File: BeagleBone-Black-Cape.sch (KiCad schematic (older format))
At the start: 2 parts, among them P8 BeagleBone_Black_Header, P9 BeagleBone_Black_Header

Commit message: Added Buttons, LEDs and MCU to BB connections.
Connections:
- net labels added: BB_BTN_1, BB_BTN_2, PWR_BTN, ZNP_RX, ZNP_TX
- net labels removed: PWR_BUT
- wire segments 39 -> 43
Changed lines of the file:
@@
 	2450 1800 2550 1800
 Text GLabel 1850 1800 0    50   Input ~ 0
-PWR_BUT
+PWR_BTN
 Wire Wire Line
 	1950 1800 1850 1800
@@
 F1 "CrystolOscillator.sch" 50
 $EndSheet
+Text GLabel 1850 1900 0    50   Input ~ 0
+ZNP_TX
+Text GLabel 1850 2000 0    50   Input ~ 0
+ZNP_RX
+Wire Wire Line
+	1850 1900 1950 1900
+Wire Wire Line
+	1850 2000 1950 2000
+Text GLabel 2550 2000 2    50   Input ~ 0
+BB_BTN_1
+Text GLabel 2550 2100 2    50   Input ~ 0
+BB_BTN_2
+Wire Wire Line
+	2550 2000 2450 2000
+Wire Wire Line
+	2550 2100 2450 2100
 $EndSCHEMATC

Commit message: part way through getting new ICs and other components back on the PCB
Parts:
- renumbered P9 to P101, P8 to P102
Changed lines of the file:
@@
 $EndDescr
 $Comp
-L BeagleBone-Black-Cape-rescue:GNDD-power #PWR01
+L BeagleBone-Black-Cape-rescue:GNDD-power #PWR0105
 U 1 1 5589785A
 P 2200 3900
-F 0 "#PWR01" H 2200 3650 50  0001 C CNN
+F 0 "#PWR0105" H 2200 3650 50  0001 C CNN
 F 1 "GNDD" H 2200 3750 50  0000 C CNN
 F 2 "" H 2200 3900 60  0000 C CNN
@@
 Connection ~ 2200 3800
 $Comp
-L BeagleBone-Black-Cape-rescue:GNDD-power #PWR02
+L BeagleBone-Black-Cape-rescue:GNDD-power #PWR0111
 U 1 1 558978D3
 P 3250 1400
-F 0 "#PWR02" H 3250 1150 50  0001 C CNN
+F 0 "#PWR0111" H 3250 1150 50  0001 C CNN
 F 1 "GNDD" H 3250 1250 50  0000 C CNN
 F 2 "" H 3250 1400 60  0000 C CNN
@@
 $EndComp
 $Comp
-L BeagleBone-Black-Cape-rescue:GNDD-power #PWR03
+L BeagleBone-Black-Cape-rescue:GNDD-power #PWR0101
 U 1 1 5589790A
 P 1150 1400
-F 0 "#PWR03" H 1150 1150 50  0001 C CNN
+F 0 "#PWR0101" H 1150 1150 50  0001 C CNN
 F 1 "GNDD" H 1150 1250 50  0000 C CNN
 F 2 "" H 1150 1400 60  0000 C CNN
@@
 $EndComp
 $Comp
-L BeagleBone-Black-Cape-rescue:GNDD-power #PWR04
+L BeagleBone-Black-Cape-rescue:GNDD-power #PWR0112
 U 1 1 558979C1
 P 9850 750
-F 0 "#PWR04" H 9850 500 50  0001 C CNN
+F 0 "#PWR0112" H 9850 500 50  0001 C CNN
 F 1 "GNDD" H 9850 600 50  0000 C CNN
 F 2 "" H 9850 750 60  0000 C CNN
@@
 $EndComp
 $Comp
-L BeagleBone-Black-Cape-rescue:GNDD-power #PWR05
+L BeagleBone-Black-Cape-rescue:GNDD-power #PWR0113
 U 1 1 558979E8
 P 10850 750
-F 0 "#PWR05" H 10850 500 50  0001 C CNN
+F 0 "#PWR0113" H 10850 500 50  0001 C CNN
 F 1 "GNDD" H 10850 600 50  0000 C CNN
 F 2 "" H 10850 750 60  0000 C CNN
@@
 $EndComp
 $Comp
-L BeagleBone-Black-Cape-rescue:+3.3V-power #PWR06
+L BeagleBone-Black-Cape-rescue:+3.3V-power #PWR0106
 U 1 1 55897A67
 P 2600 1200
-F 0 "#PWR06" H 2600 1050 50  0001 C CNN
+F 0 "#PWR0106" H 2600 1050 50  0001 C CNN
 F 1 "+3V3" H 2600 1340 50  0000 C CNN
 F 2 "" H 2600 1200 60  0000 C CNN
@@
 $EndComp
 $Comp
-L BeagleBone-Black-Cape-rescue:+5V-power #PWR07
+L BeagleBone-Black-Cape-rescue:+5V-power #PWR0107
 U 1 1 55897A7F
 P 2800 1200
-F 0 "#PWR07" H 2800 1050 50  0001 C CNN
+F 0 "#PWR0107" H 2800 1050 50  0001 C CNN
 F 1 "+5V" H 2800 1340 50  0000 C CNN
 F 2 "" H 2800 1200 60  0000 C CNN
@@
 	3050 1700 2450 1700
 $Comp
-L BeagleBone-Black-Cape-rescue:+3.3V-power #PWR08
+L BeagleBone-Black-Cape-rescue:+3.3V-power #PWR0104
 U 1 1 55897EE7
 P 1800 1200
-F 0 "#PWR08" H 1800 1050 50  0001 C CNN
+F 0 "#PWR0104" H 1800 1050 50  0001 C CNN
 F 1 "+3V3" H 1800 1340 50  0000 C CNN
 F 2 "" H 1800 1200 60  0000 C CNN
@@
 $EndComp
 $Comp
-L BeagleBone-Black-Cape-rescue:+5V-power #PWR09
+L BeagleBone-Black-Cape-rescue:+5V-power #PWR0103
 U 1 1 55897EF8
 P 1600 1200
-F 0 "#PWR09" H 1600 1050 50  0001 C CNN
+F 0 "#PWR0103" H 1600 1050 50  0001 C CNN
 F 1 "+5V" H 1600 1340 50  0000 C CNN
 F 2 "" H 1600 1200 60  0000 C CNN
@@
 	10600 750  10850 750
 $Comp
-L pwr_BeagleBone:SYS_5V #PWR010
+L pwr_BeagleBone:SYS_5V #PWR0110
 U 1 1 55898497
 P 3050 1200
-F 0 "#PWR010" H 3050 1050 50  0001 C CNN
+F 0 "#PWR0110" H 3050 1050 50  0001 C CNN
 F 1 "SYS_5V" H 3050 1340 50  0000 C CNN
 F 2 "" H 3050 1200 60  0000 C CNN
@@
 $EndComp
 $Comp
-L pwr_BeagleBone:SYS_5V #PWR011
+L pwr_BeagleBone:SYS_5V #PWR0102
 U 1 1 558984AF
 P 1350 1200
-F 0 "#PWR011" H 1350 1050 50  0001 C CNN
+F 0 "#PWR0102" H 1350 1050 50  0001 C CNN
 F 1 "SYS_5V" H 1350 1340 50  0000 C CNN
 F 2 "" H 1350 1200 60  0000 C CNN
@@
 	2450 2900 2800 2900
 $Comp
-L pwr_BeagleBone:GNDA_ADC #PWR013
+L pwr_BeagleBone:GNDA_ADC #PWR0109
 U 1 1 5589865D
 P 2800 3000
-F 0 "#PWR013" H 2800 2750 50  0001 C CNN
+F 0 "#PWR0109" H 2800 2750 50  0001 C CNN
 F 1 "GNDA_ADC" H 2700 2850 50  0000 C CNN
 F 2 "" H 2800 3000 60  0000 C CNN
@@
 	1950 1800 1850 1800
 $Comp
-L BeagleBone-Black-Cape-rescue:Conn_02x23_Odd_Even-Connector_Generic P9
+L BeagleBone-Black-Cape-rescue:Conn_02x23_Odd_Even-Connector_Generic P101
 U 1 1 55DF7DBA
 P 2150 2500
-F 0 "P9" H 2150 3700 50  0000 C CNN
+F 0 "P101" H 2150 3700 50  0000 C CNN
 F 1 "BeagleBone_Black_Header" V 2200 2550 50  0000 C CNN
 F 2 "Socket_BeagleBone_Black:Socket_BeagleBone_Black" H 2150 1650 60  0001 C CNN
@@
 $EndComp
 $Comp
-L BeagleBone-Black-Cape-rescue:Conn_02x23_Odd_Even-Connector_Generic P8
+L BeagleBone-Black-Cape-rescue:Conn_02x23_Odd_Even-Connector_Generic P102
 U 1 1 55DF7DE1
 P 10300 1850
-F 0 "P8" H 10300 3050 50  0000 C CNN
+F 0 "P102" H 10300 3050 50  0000 C CNN
 F 1 "BeagleBone_Black_Header" V 10350 1900 50  0000 C CNN
 F 2 "Socket_BeagleBone_Black:Socket_BeagleBone_Black" H 10300 1000 60  0001 C CNN
@@
 MOSI_TFT
 $Comp
-L pwr_BeagleBone:VDD_ADC #PWR012
+L pwr_BeagleBone:VDD_ADC #PWR0108
 U 1 1 558985D8
 P 2800 2900
-F 0 "#PWR012" H 2800 2750 50  0001 C CNN
+F 0 "#PWR0108" H 2800 2750 50  0001 C CNN
 F 1 "VDD_ADC" H 2800 3150 50  0000 C CNN
 F 2 "" H 2800 2900 60  0000 C CNN

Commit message: Added UI buttons, LEDs, Decoupling caps, MCU connections, and other good stuff.
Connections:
- net labels added: GND
- net labels removed: GND8, GNDA_ADC, GNDD, VDD_ADC
- wire segments 43 -> 38
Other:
- moved on the sheet: P101, P102

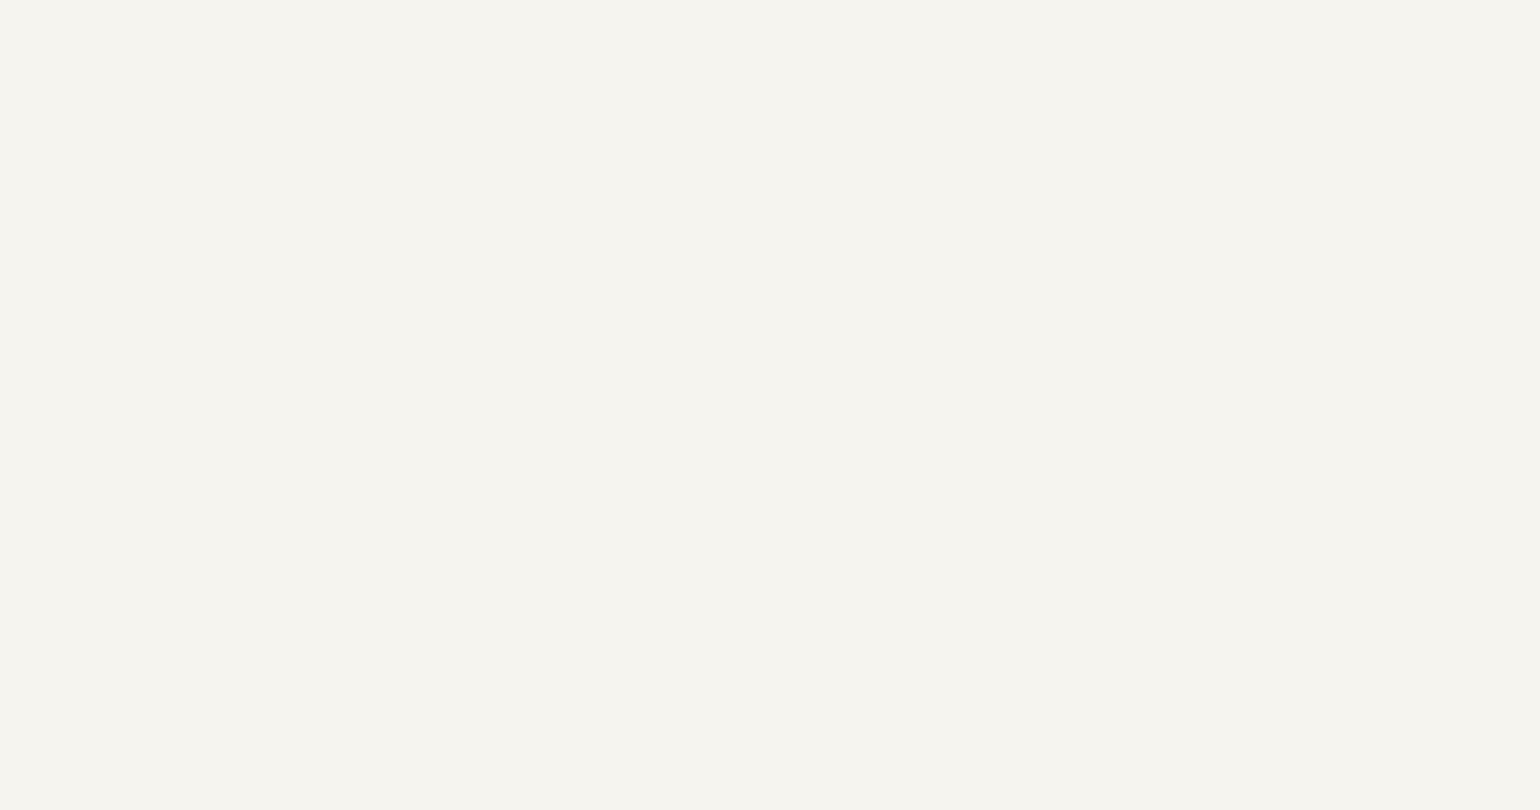
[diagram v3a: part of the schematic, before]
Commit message: Moved MCU to its own sheet.
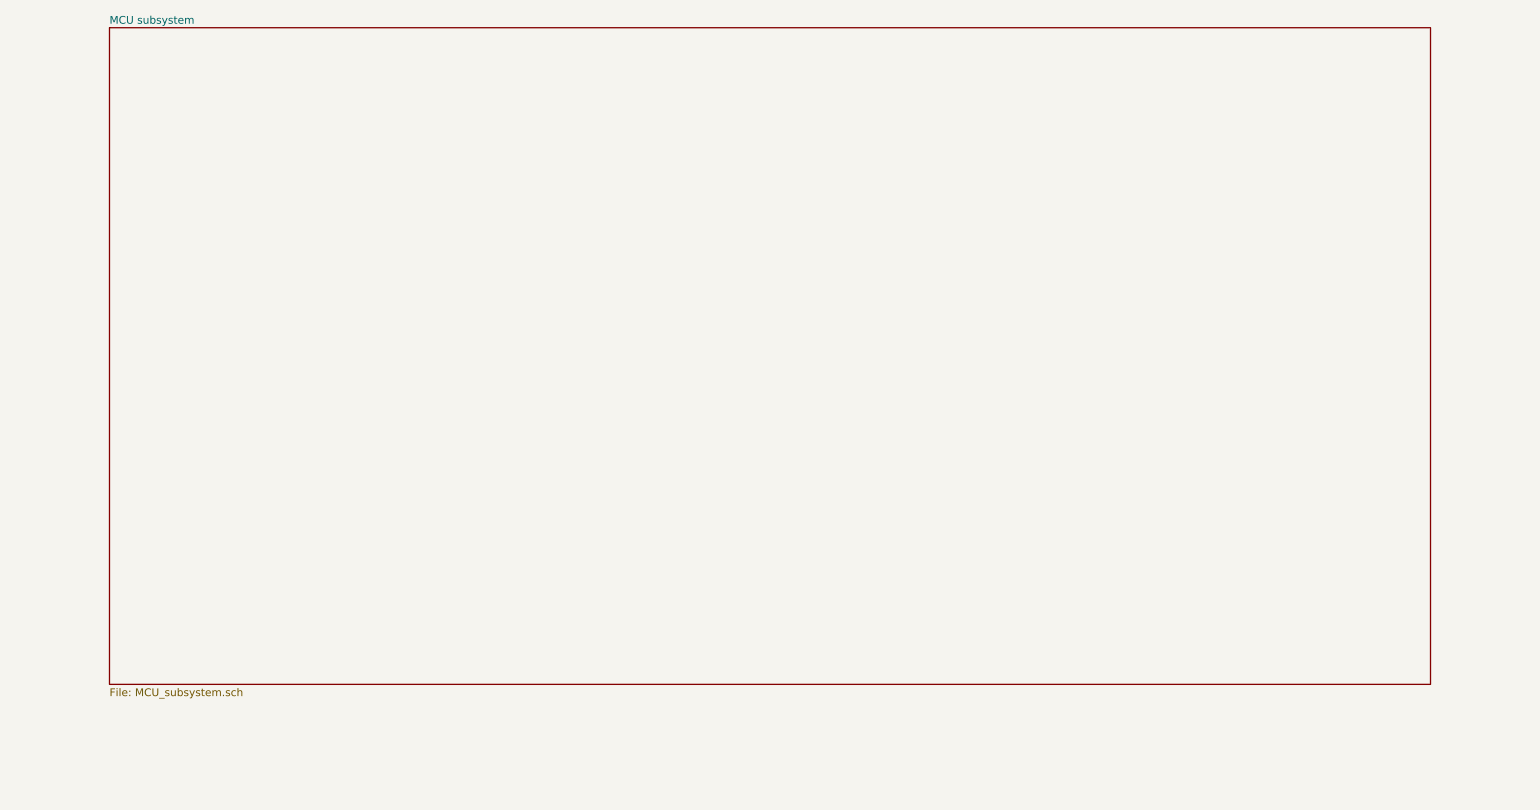
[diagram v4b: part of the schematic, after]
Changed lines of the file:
@@
 $Descr A4 11693 8268
 encoding utf-8
-Sheet 1 6
+Sheet 1 7
 Title ""
 Date ""
@@
 	1    0    0    -1
 $EndComp
+$Sheet
+S 2000 -4750 8550 4250
+U 614C2CA1
+F0 "MCU subsystem" 50
+F1 "MCU_subsystem.sch" 50
+$EndSheet
 $EndSCHEMATC

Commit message: Finished Adding MCU connections and combined crystal and MCU sheets.
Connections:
- net BB_LED_1: now reaches P101.24 (Pin_24)
- net BB_LED_2: now reaches P101.26 (Pin_26)
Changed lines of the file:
@@
 $Descr A4 11693 8268
 encoding utf-8
-Sheet 1 7
+Sheet 1 6
 Title ""
 Date ""
@@
 	4450 4700 4450 4900
 $Sheet
-S 250  8450 11700 8250
+S 12500 6450 9850 5200
 U 60365D6B
 F0 "1352_antenna_subsystem" 50
@@
 	3600 3200 3800 3200
 $Sheet
-S -12100 2000 11950 7750
+S 12450 12300 8350 4400
 U 60837686
 F0 "UI_subsystem" 50
@@
 $EndSheet
 $Sheet
-S 13500 3750 7500 3800
+S 12900 2050 7500 3800
 U 610F5588
 F0 "Power Sub System" 50
 F1 "PowerSubSystem.sch" 50
-$EndSheet
-$Sheet
-S 14700 -300 5600 3550
-U 613805C9
-F0 "CrystolOscillator" 50
-F1 "CrystolOscillator.sch" 50
 $EndSheet
 Text GLabel 3700 3000 0    50   Input ~ 0
@@
 	4400 3200 4300 3200
 $Sheet
-S -9700 -4300 8100 5100
+S 12850 -2600 7900 4050
 U 614A9A85
 F0 "Debug subsystem" 50
@@
 $EndComp
 $Sheet
-S 2000 -4750 8550 4250
+S 12900 -7450 8550 4250
 U 614C2CA1
 F0 "MCU subsystem" 50
 F1 "MCU_subsystem.sch" 50
 $EndSheet
+Text GLabel 4450 3600 2    50   Output ~ 0
+BB_LED_1
+Text GLabel 4450 3700 2    50   Output ~ 0
+BB_LED_2
+Wire Wire Line
+	4300 3600 4450 3600
+Wire Wire Line
+	4300 3700 4450 3700
 $EndSCHEMATC
